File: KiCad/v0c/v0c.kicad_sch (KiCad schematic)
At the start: 25 parts, among them U1 AM29F160, U10 IS62C256AL, U2 74HC139, U3 74HC273, U4 74HC191, U5 74HC191, U6 74HC191, U7 74HC670, U8 74HC00, U9 IS62C256AL

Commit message: sam2695 on board
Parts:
- added C15, C16, C21: C_Small, Capacitor_SMD:C_0603_1608Metric_Pad1.08x0.95mm_HandSolder, symbol Device:C_Small
- added C17: 1µF, Capacitor_SMD:C_0805_2012Metric_Pad1.18x1.45mm_HandSolder, symbol Device:C_Polarized
- added C18, C20: C_Small, Capacitor_SMD:C_0805_2012Metric_Pad1.18x1.45mm_HandSolder, symbol Device:C_Small
- added C19, C2: 1µF, Capacitor_SMD:C_0805_2012Metric_Pad1.18x1.45mm_HandSolder, symbol Device:C_Small
- added R2: 100Ω, PCM_Resistor_SMD_AKL:R_0603_1608Metric_Pad1.05x0.95mm_HandSolder, symbol Device:R_Small
- added R3: 47KΩ, PCM_Resistor_SMD_AKL:R_0603_1608Metric_Pad1.05x0.95mm_HandSolder, symbol Device:R_Small
- added R4: 4.7K, PCM_Resistor_SMD_AKL:R_0603_1608Metric_Pad1.05x0.95mm_HandSolder, symbol Device:R_Small
- added U11: SAM2695, Package_DFN_QFN:QFN-48-1EP_6x6mm_P0.4mm_EP4.2x4.2mm, symbol Smal:SAM2695
- added U12: MCP1700, Package_TO_SOT_SMD:SOT-89-3_Handsoldering, symbol Regulator_Linear:MCP1700x-330xxTO
- added Y1: 12M, Crystal:Crystal_HC49-4H_Vertical, symbol Device:Crystal
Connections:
- net GND: now also C15.2, C16.2, C18.2, C19.2, C2.2, C20.1, C21.2, R3.2, U11.13 (GND), U11.18 (GND), U11.25 (GND), U11.36 (GND), U11.4 (AGND), U11.45 (GND), U11.48 (GND), U11.49 (GND_DIE), U11.9 (GND), U12.1 (GND)
- net VCC: now also C19.1, U12.2 (VI)
- net cA0: now also U11.10 (A0)
- net cD0: now also U11.24 (D0)
- net cD1: now also U11.26 (D1)
- net cD2: now also U11.27 (D2)
- net cD3: now also U11.28 (D3)
- net cD4: now also U11.29 (D4)
- net cD5: now also U11.30 (D5)
- net cD6: now also U11.32 (D6)
- net cD7: now also U11.33 (D7)
- net ~{RESET}: now also U11.38 (~{RST}/~{PD})
- net ~{SoundCS}: now also U11.14 (~{CS})
- net ~{samWr}: now also U11.12 (~{WR})
- net rfAUDIO: now reaches H1.45 (cAUDIO), H1.46 (rfAUDIO)
- net rfAUDIO: now also R2.1
- new net: C17.2, R2.2, R3.1
- new net: C17.1, U11.1 (AOUTL)
- new net: C18.1, U11.34 (OUTVC12)
- new net: C16.1, U11.39 (X1), Y1.2
- new net: C21.1, U11.40 (X2), Y1.1
- new net: C15.1, C20.2, U11.5 (VCM)
- new net: R4.2, U11.6 (VAD33)
- new net +3V3: C2.1, R4.1, U11.11 (VD33), U11.15 (~{RD}), U11.20 (VD33), U11.31 (VD33), U11.35 (VD33), U11.41 (VD33), U11.46 (VD33), U11.47 (XDIV), U11.8 (VD33), U12.3 (VO)
- no-connect marks 24 -> 30
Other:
- note added: "Sound Expansion"

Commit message: Silkscreen and schematic tweaks
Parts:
- removed C15, C16, C21: C_Small, Capacitor_SMD:C_0603_1608Metric_Pad1.08x0.95mm_HandSolder, symbol Device:C_Small
- removed C17: 1µF, Capacitor_SMD:C_0805_2012Metric_Pad1.18x1.45mm_HandSolder, symbol Device:C_Polarized
- removed C18, C20: C_Small, Capacitor_SMD:C_0805_2012Metric_Pad1.18x1.45mm_HandSolder, symbol Device:C_Small
- removed C19, C2: 1µF, Capacitor_SMD:C_0805_2012Metric_Pad1.18x1.45mm_HandSolder, symbol Device:C_Small
- removed R2: 100Ω, PCM_Resistor_SMD_AKL:R_0603_1608Metric_Pad1.05x0.95mm_HandSolder, symbol Device:R_Small
- removed R3: 47KΩ, PCM_Resistor_SMD_AKL:R_0603_1608Metric_Pad1.05x0.95mm_HandSolder, symbol Device:R_Small
- removed R4: 4.7K, PCM_Resistor_SMD_AKL:R_0603_1608Metric_Pad1.05x0.95mm_HandSolder, symbol Device:R_Small
- removed U11: SAM2695, Package_DFN_QFN:QFN-48-1EP_6x6mm_P0.4mm_EP4.2x4.2mm, symbol Smal:SAM2695
- removed U12: MCP1700, Package_TO_SOT_SMD:SOT-89-3_Handsoldering, symbol Regulator_Linear:MCP1700x-330xxTO
- removed Y1: 12M, Crystal:Crystal_HC49-4H_Vertical, symbol Device:Crystal
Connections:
- no-connect marks 30 -> 24
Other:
- added sheet Sound (sound.kicad_sch)
- note added: "* 2048KiB PRG FLASH (rewrittable), 32KiB Window * 32KiB PRG RAM, 8KiB Window * 32KiB CHR RAM, 4x4KiB Window * Four-Screen Scrolling * Scanline IRQ * SAM2695 Sound Expansion"
- note removed: "* 2048KiB PRG FLASH (rewrittable), 32KiB Window * 32KiB PRG RAM, 8KiB Window * 32KiB CHR RAM, 4x4KiB Window * Four-Screen Scrolling * Scanline IRQ"
- note removed: "Sound Expansion"

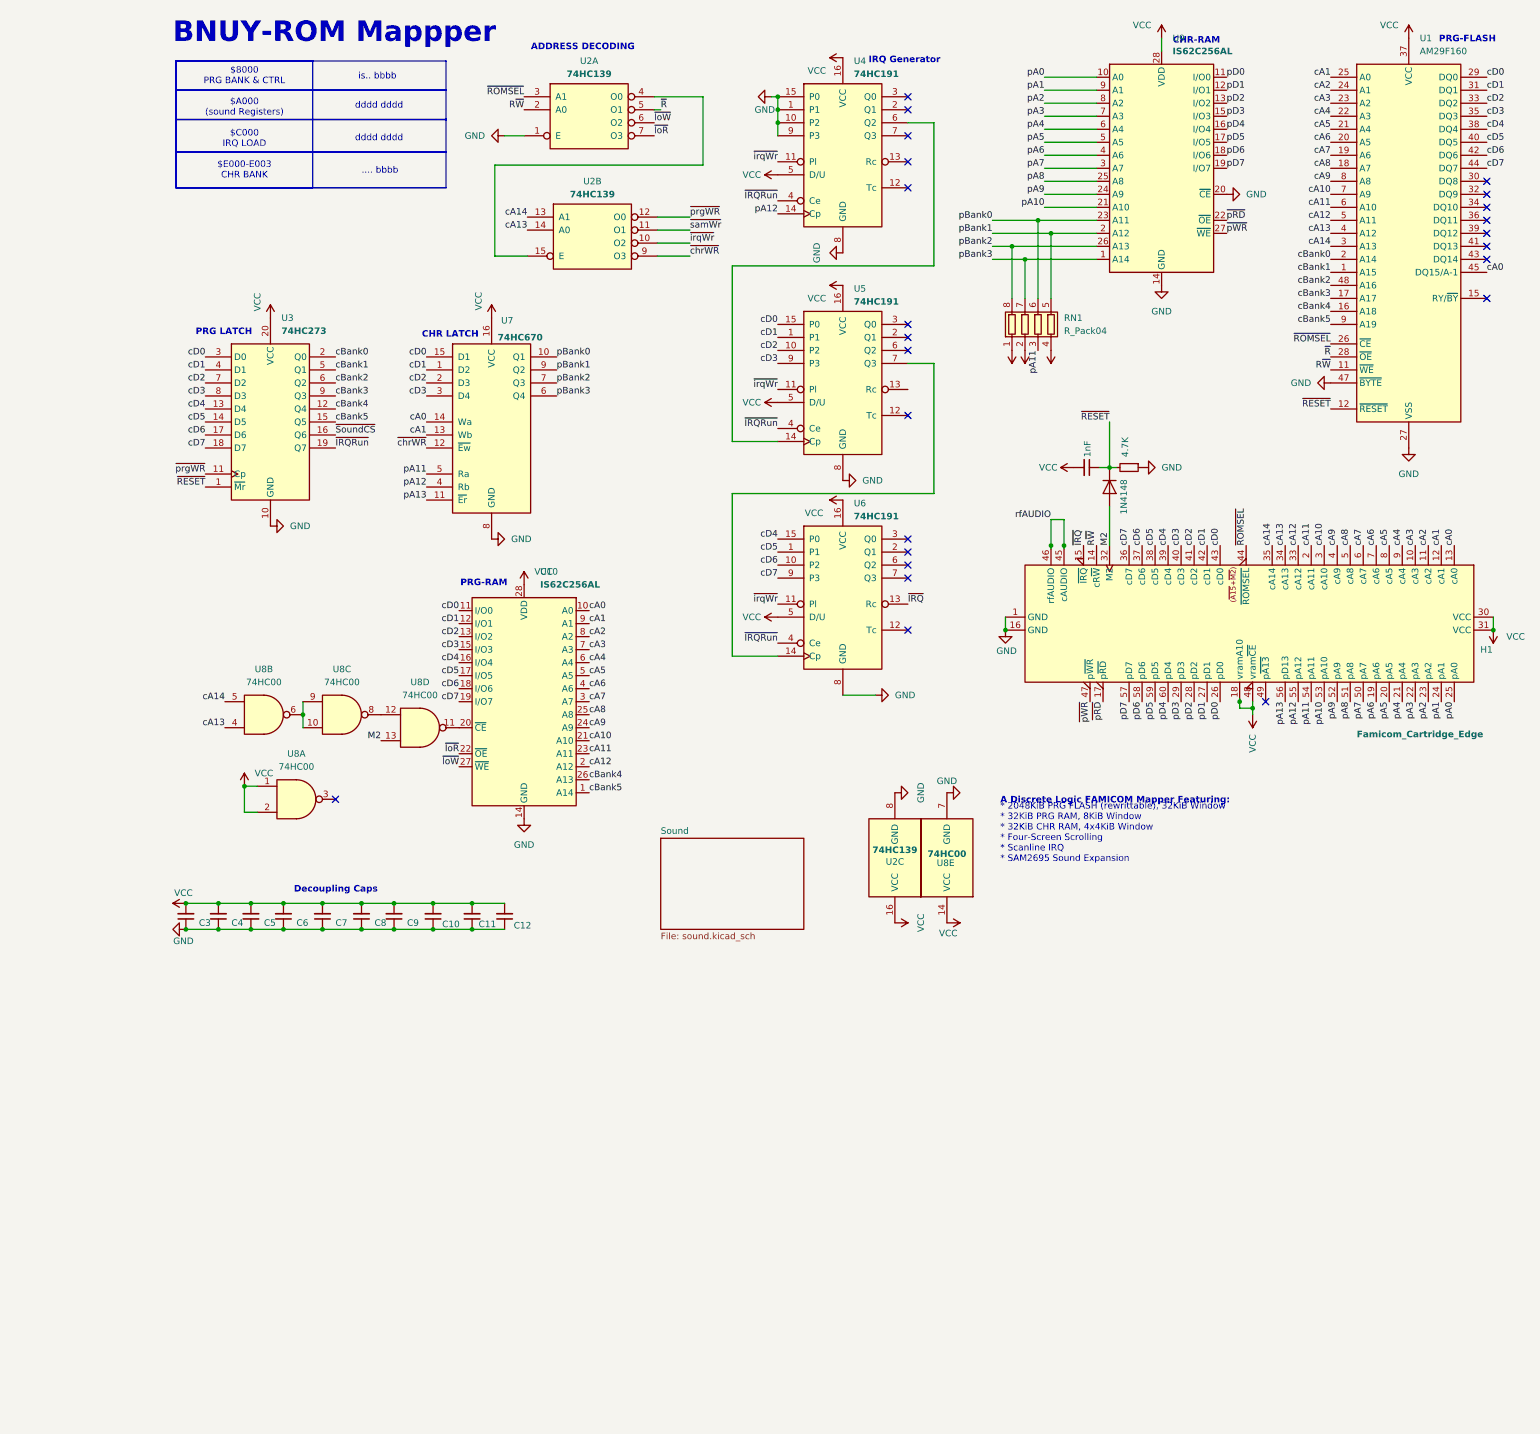
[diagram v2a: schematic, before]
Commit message: Change Scanline Circuit
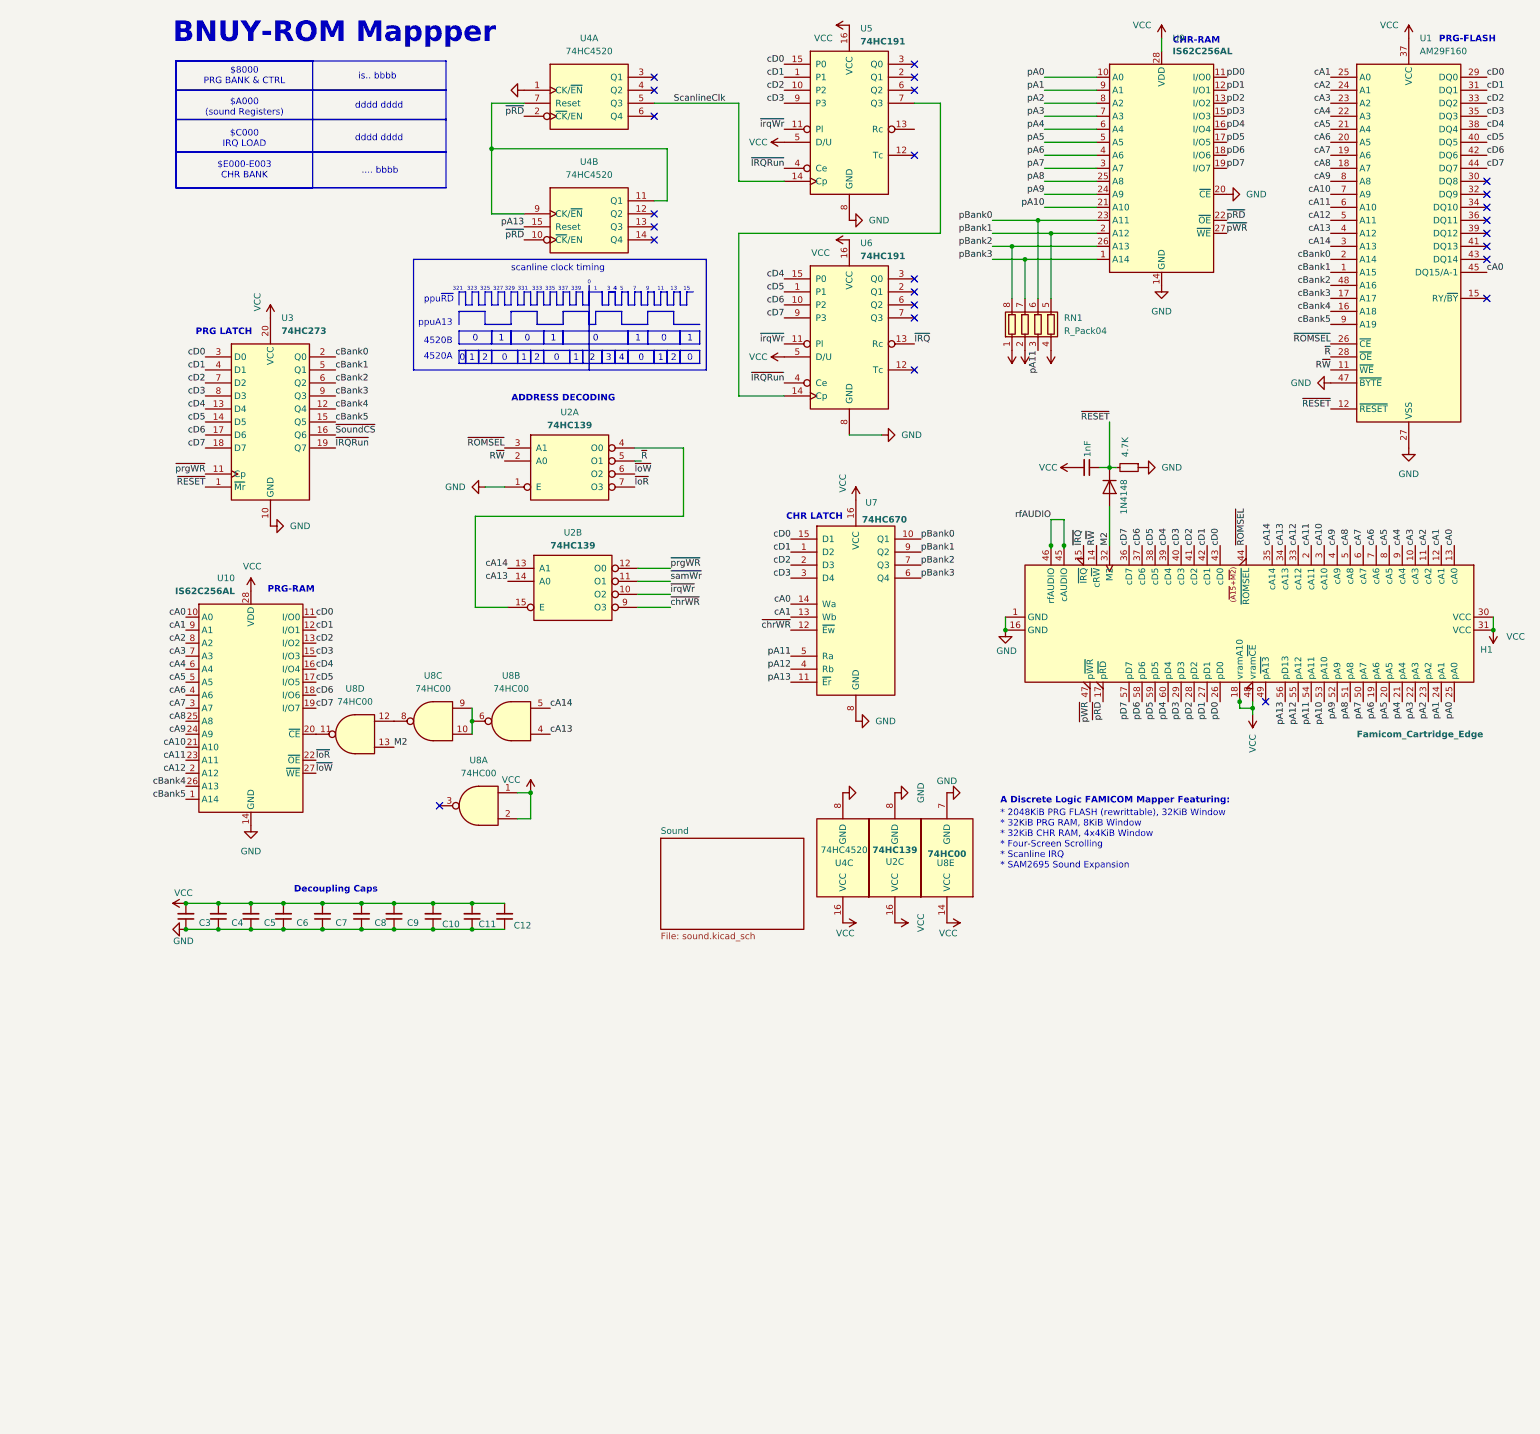
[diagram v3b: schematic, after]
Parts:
- removed U4: 74HC191, Package_SO:SOIC-16_3.9x9.9mm_P1.27mm, symbol 74xx:74LS191
- added U4: 74HC4520, Package_SO:SOIC-16_3.9x9.9mm_P1.27mm, symbol 4xxx:4520
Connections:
- net GND: now also U4.1 (CK/~{EN}), U4.8 (GND)
- net VCC: now also U4.16 (VCC)
- net pA13: now also U4.15 (Reset)
- net ~{pRD}: now also U4.10 (~{CK}/EN), U4.2 (~{CK}/EN)
- net ScanlineClk: now reaches U5.14 (Cp)
- net ScanlineClk: now also U4.5 (Q3)
- new net: U4.11 (Q1), U4.7 (Reset), U4.9 (CK/~{EN})
- no-connect marks 24 -> 25
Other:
- note added: "0"
- note added: "1"
- note added: "11"
- note added: "13"
- note added: "15"
- note added: "3"
- note added: "321"
- note added: "323"
- note added: "325"
- note added: "327"
- note added: "329"
- note added: "331"
- note added: "333"
- note added: "335"
- note added: "337"
- note added: "339"
- note added: "4"
- note added: "4520A"
- note added: "4520B"
- note added: "5"
- note added: "7"
- note added: "9"
- note added: "ppuA13"
- note added: "ppu~{RD}"
- note added: "scanline clock timing"
- note removed: "IRQ Generator"
- moved on the sheet: U10, U2A, U2B, U5, U6, U7, U8A, U8B, U8C, U8D

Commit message: Update pcbs and readme
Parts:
- removed C12: C_Small, Capacitor_SMD:C_0603_1608Metric_Pad1.08x0.95mm_HandSolder, symbol Device:C_Small
- removed U5, U6: 74HC191, Package_SO:SOIC-16_3.9x9.9mm_P1.27mm, symbol 74xx:74LS191
- added U13: 74HC40103, Package_SO:SOIC-16_3.9x9.9mm_P1.27mm, symbol 74xxEX:74HC40103
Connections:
- net GND: now also U13.3 (~{TE}), U13.8 (GND)
- net ScanlineClk: now also U13.1 (CP)
- net VCC: now also U13.15 (~{PE}), U13.16 (VCC)
- net cD0: now also U13.4 (P0)
- net cD1: now also U13.5 (P1)
- net cD2: now also U13.6 (P2)
- net cD3: now also U13.7 (P3)
- net cD4: now also U13.10 (P4)
- net cD5: now also U13.11 (P5)
- net cD6: now also U13.12 (P6)
- net cD7: now also U13.13 (P7)
- net ~{IRQRun}: now also U13.2 (~{MR})
- net ~{IRQ}: now also U13.14 (~{TC})
- net ~{irqWr}: now also U13.9 (~{PL})
- net rfAUDIO renamed rfAudio
- no-connect marks 25 -> 16
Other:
- moved on the sheet: U2B
